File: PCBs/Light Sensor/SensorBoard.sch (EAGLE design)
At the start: 7 parts, among them J1 AVR_SPI_PRG_6NS, U1 TINY85-20-DIP

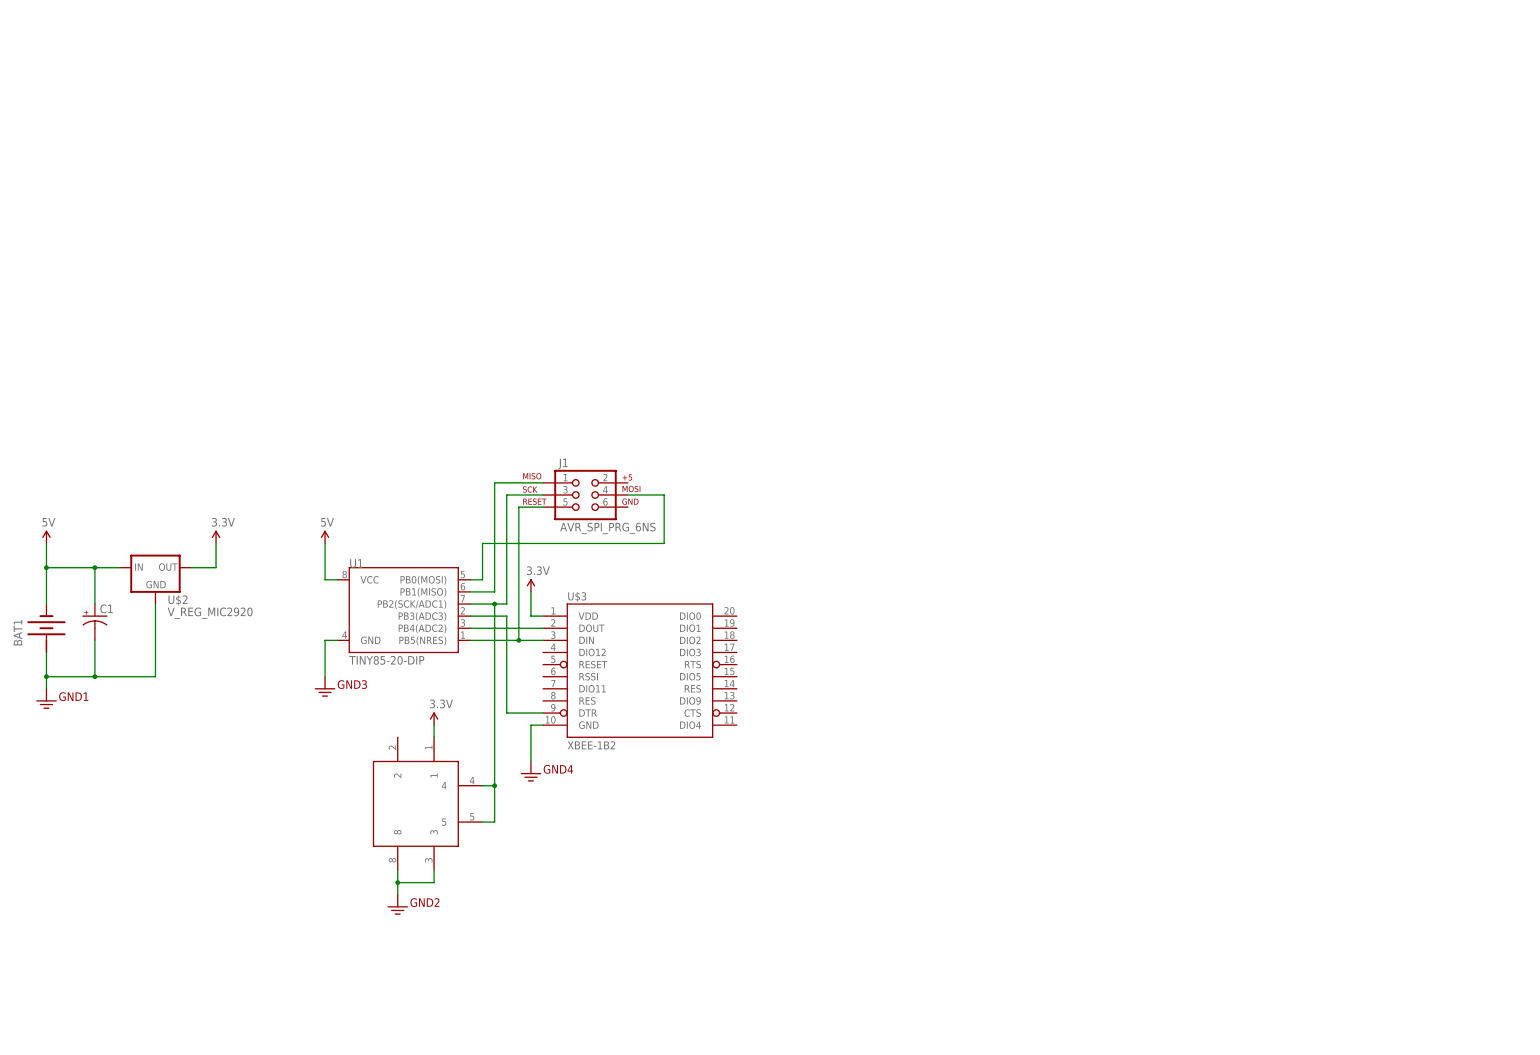
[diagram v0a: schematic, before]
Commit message: Changed to using breadboard friendly symbols
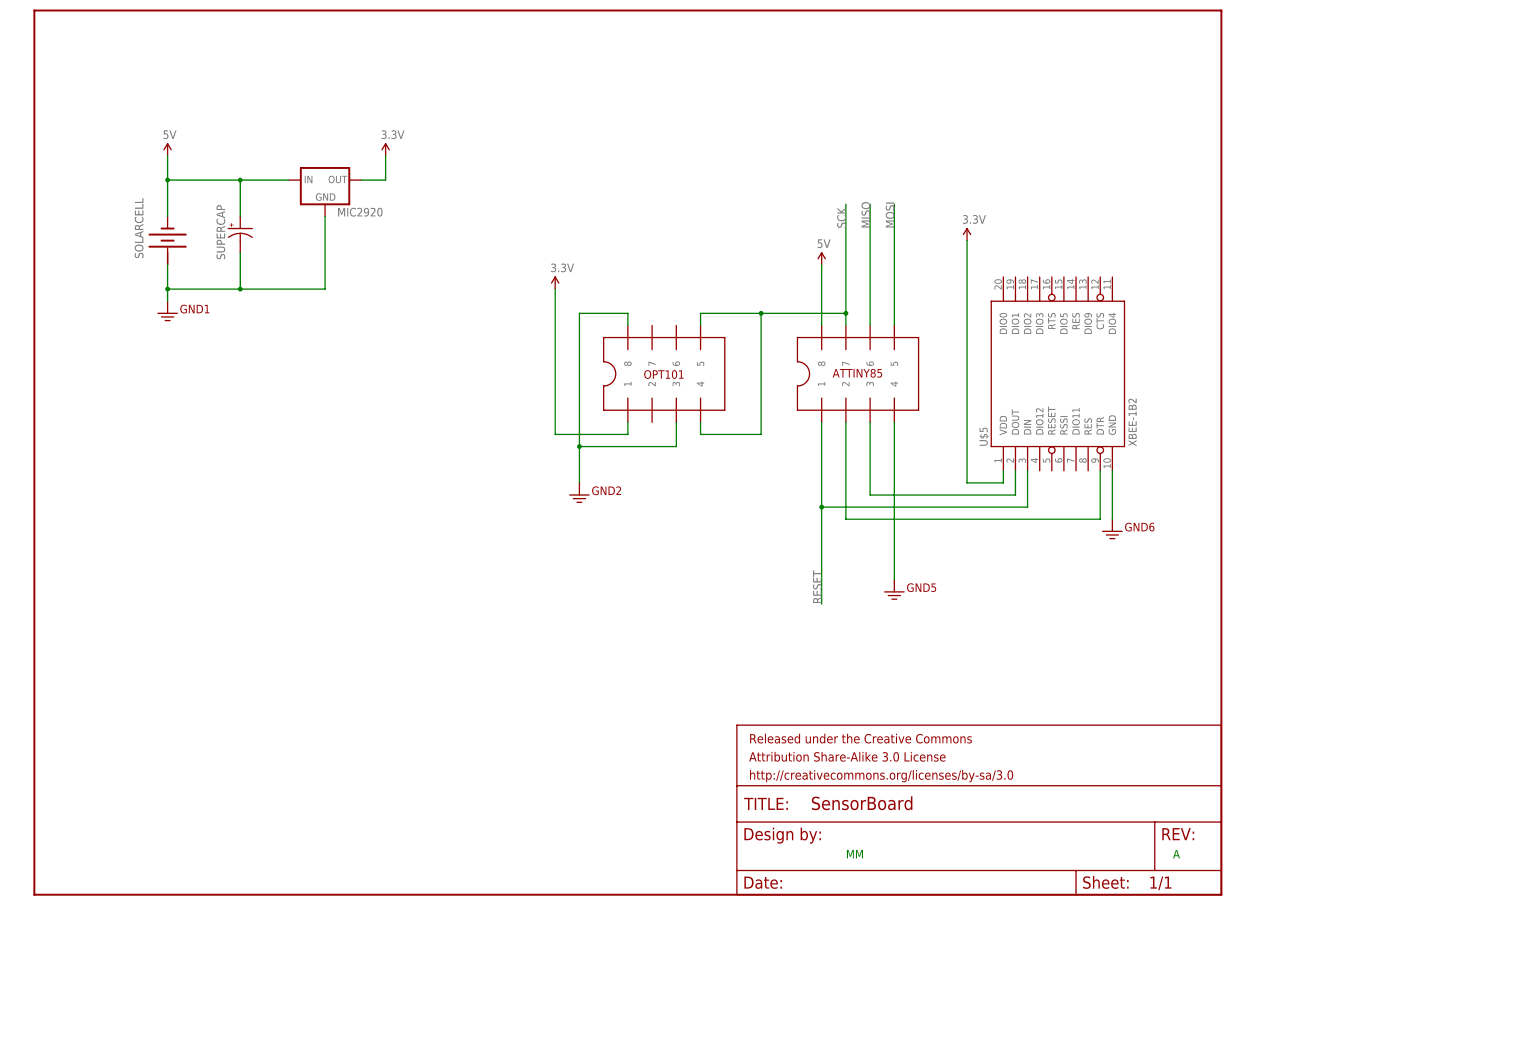
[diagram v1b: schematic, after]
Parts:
- removed BAT1: (no value), special:BATTERY
- removed C1: (no value), rcl:CPOL-USE55-30AXIAL
- removed J1: AVR_SPI_PRG_6NS, SparkFun-Connectors:AVR_SPI_PRG_6NS
- removed U$2: V_REG_MIC2920, SparkFun-PowerIC:V_REG_MIC2920
- removed U$3: XBEE-1B2, SparkFun-RF:XBEE-1B2
- removed U1: TINY85-20-DIP, SparkFun-DigitalIC:ATTINY45TINY85-20-DIP
- added FRAME1: FRAME-LETTER, SparkFun-Aesthetics:FRAME-LETTER
- added MIC2920: V_REG_MIC2920, SparkFun-PowerIC:V_REG_MIC2920
- added SOLARCELL: (no value), special:BATTERY
- added SUPERCAP: (no value), rcl:CPOL-USE55-30AXIAL
- added U$4: ATTINY85, MyLibrary:ATTINY85
- added U$5: XBEE-1B2, SparkFun-RF:XBEE-1B2
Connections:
- removed net N$1: U$3.DOUT, U1.PB4(ADC2)
- removed net N$2: J1.3, U$1.4, U$1.5, U1.PB2(SCK/ADC1)
- removed net N$3: J1.5, U$3.DIN, U1.PB5(NRES)
- removed net N$4: U$3.DTR, U1.PB3(ADC3)
- removed net N$5: J1.1, U1.PB1(MISO)
- removed net N$7: J1.4, U1.PB0(MOSI)
- new net MISO: U$4.6
- new net MOSI: U$4.5
- new net N$10: U$4.3, U$5.DOUT
- new net N$8: U$4.2, U$5.DTR
- new net RESET: U$4.1, U$5.DIN
- new net SCK: U$1.4, U$1.5, U$4.7
- net 3.3V: now also MIC2920.GND, MIC2920.OUT, SOLARCELL.+, SUPERCAP.-, U$4.4, U$5.GND, U$5.VDD; no longer BAT1.+, C1.-, U$2.GND, U$2.OUT, U$3.GND, U$3.VDD, U1.GND
- net 5V: now also MIC2920.IN, SOLARCELL.-, SUPERCAP.+, U$4.8; no longer BAT1.-, C1.+, U$2.IN, U1.VCC
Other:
- note added: "A"
- note added: "MM"

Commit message: Added level translator, jumpers
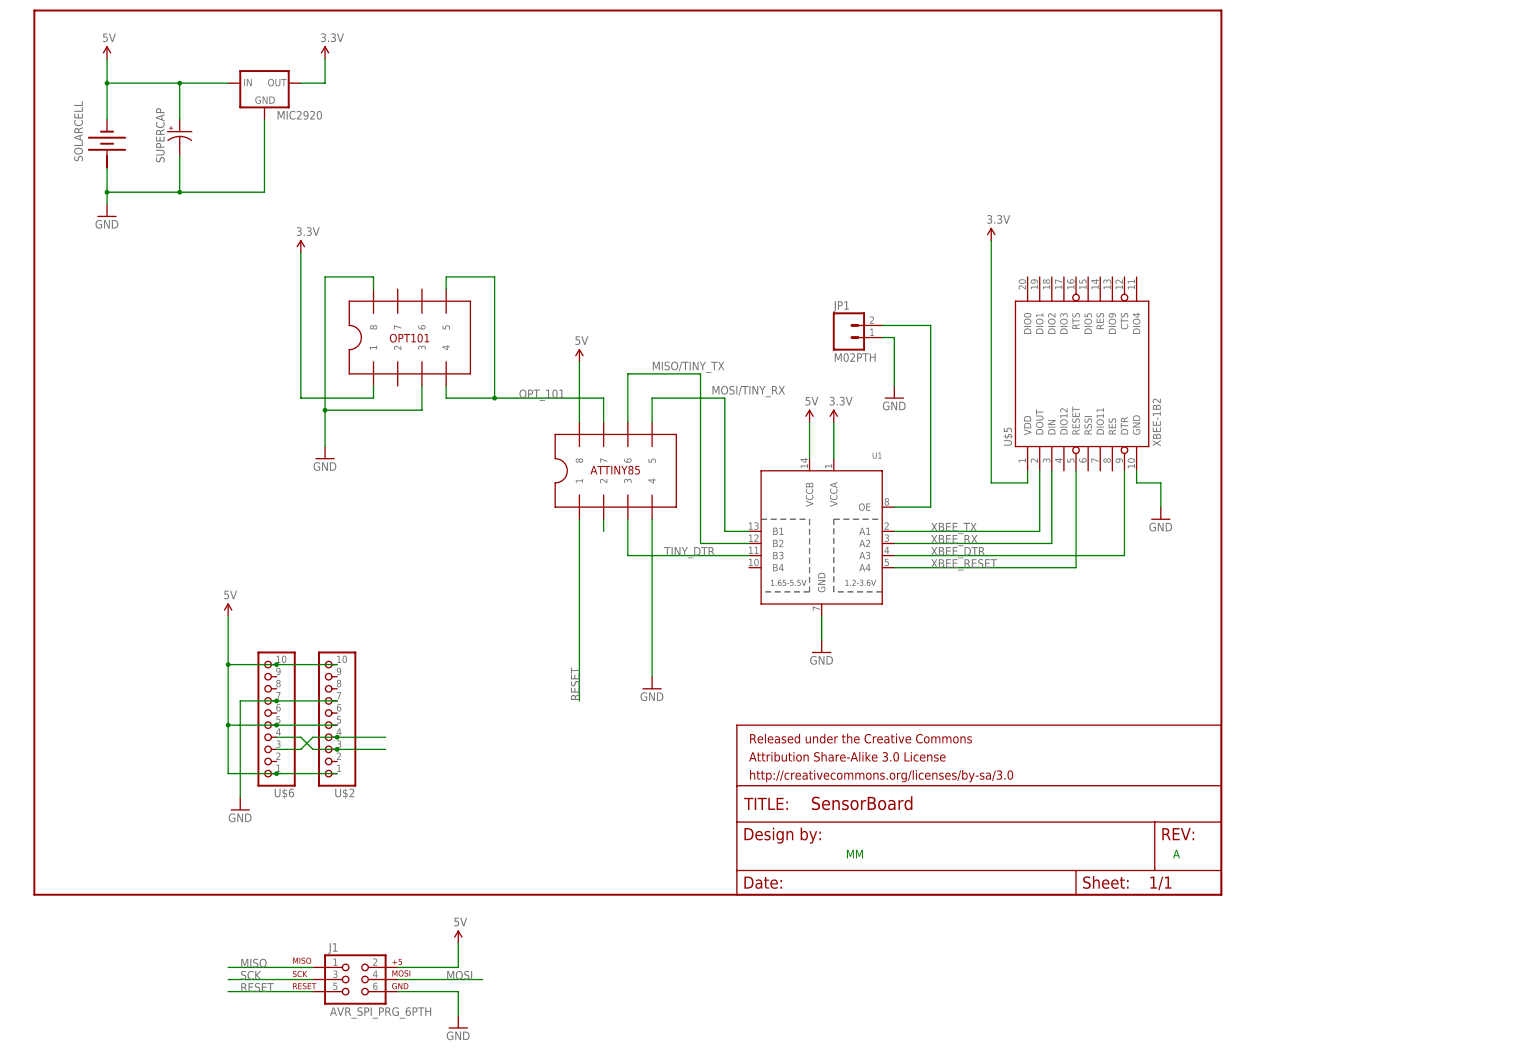
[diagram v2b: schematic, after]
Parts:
- added J1: AVR_SPI_PRG_6PTH, SparkFun-Connectors:AVR_SPI_PRG_6PTH
- added JP1: M02PTH, SparkFun-Connectors:M02PTH
- added U$2, U$6: PINHD-1X10, adafruit:PINHD-1X10
- added U1: (no value), SparkFun-DigitalIC:TXB0104PWRSOIC14
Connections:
- removed net N$10: U$4.3, U$5.DOUT
- removed net N$8: U$4.2, U$5.DTR
- new net GND: J1.6, JP1.1, MIC2920.GND, SOLARCELL.+, SUPERCAP.-, U$1.3, U$1.8, U$2.7, U$4.4, U$5.GND, U$6.7, U1.GND
- new net MISO/TINY_TX: U$4.6, U1.B2
- new net MOSI/TINY_RX: U$4.5, U1.B1
- new net N$2: U$2.3, U$6.4
- new net N$3: U$2.4, U$6.3
- new net N$5: JP1.2, U1.OE
- new net OPT_101: U$1.4, U$1.5, U$4.7
- new net TINY_DTR: U$4.3, U1.B3
- new net XBEE_DTR: U$4.2, U$5.DTR, U1.A3
- new net XBEE_RESET: U$5.RESET, U1.A4
- new net XBEE_RX: U$5.DIN, U1.A2
- new net XBEE_TX: U$5.DOUT, U1.A1
- net 3.3V: now also U1.VCCA; no longer MIC2920.GND, SOLARCELL.+, SUPERCAP.-, U$1.3, U$1.8, U$4.4, U$5.GND
- net 5V: now also J1.2, U$2.1, U$2.10, U$2.5, U$6.1, U$6.10, U$6.5, U1.VCCB
- net MISO: now also J1.1; no longer U$4.6
- net MOSI: now also J1.4; no longer U$4.5
- net RESET: now also J1.5; no longer U$5.DIN
- net SCK: now also J1.3; no longer U$1.4, U$1.5, U$4.7
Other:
- moved on the sheet: MIC2920, SOLARCELL, SUPERCAP, U$5

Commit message: Cleanups
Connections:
- removed net MISO: J1.1
- removed net MOSI: J1.4
- net MISO/TINY_TX: now also J1.1
- net MOSI/TINY_RX: now also J1.4
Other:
- moved on the sheet: J1
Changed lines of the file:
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@@
 <instance part="FRAME1" gate="G$1" x="0" y="0"/>
 <instance part="FRAME1" gate="G$2" x="147.32" y="0"/>
-<instance part="J1" gate="G$1" x="66.04" y="-17.78"/>
-<instance part="SUPPLY4" gate="G$1" x="88.9" y="-10.16"/>
+<instance part="J1" gate="G$1" x="129.54" y="160.02"/>
+<instance part="SUPPLY4" gate="G$1" x="152.4" y="167.64"/>
 <instance part="GND1" gate="1" x="15.24" y="142.24"/>
 <instance part="GND2" gate="1" x="60.96" y="91.44"/>
-<instance part="GND3" gate="1" x="88.9" y="-27.94"/>
+<instance part="GND3" gate="1" x="152.4" y="149.86"/>
 <instance part="GND4" gate="1" x="129.54" y="43.18"/>
 <instance part="GND5" gate="1" x="236.22" y="78.74"/>
@@
 <segment>
 <pinref part="J1" gate="G$1" pin="2"/>
-<wire x1="76.2" y1="-15.24" x2="88.9" y2="-15.24" width="0.1524" layer="91"/>
+<wire x1="139.7" y1="162.56" x2="152.4" y2="162.56" width="0.1524" layer="91"/>
 <pinref part="SUPPLY4" gate="G$1" pin="5V"/>
-<wire x1="88.9" y1="-10.16" x2="88.9" y2="-15.24" width="0.1524" layer="91"/>
+<wire x1="152.4" y1="167.64" x2="152.4" y2="162.56" width="0.1524" layer="91"/>
 </segment>
 <segment>
@@
 <segment>
 <pinref part="J1" gate="G$1" pin="3"/>
-<wire x1="58.42" y1="-17.78" x2="40.64" y2="-17.78" width="0.1524" layer="91"/>
-<label x="43.18" y="-17.78" size="1.778" layer="95"/>
+<wire x1="121.92" y1="160.02" x2="93.98" y2="160.02" width="0.1524" layer="91"/>
+<label x="96.52" y="160.02" size="1.778" layer="95"/>
 </segment>
 </net>
@@
 <segment>
 <pinref part="J1" gate="G$1" pin="5"/>
-<wire x1="58.42" y1="-20.32" x2="40.64" y2="-20.32" width="0.1524" layer="91"/>
-<label x="43.18" y="-20.32" size="1.778" layer="95"/>
-</segment>
-</net>
-<net name="MISO" class="0">
-<segment>
-<pinref part="J1" gate="G$1" pin="1"/>
-<wire x1="58.42" y1="-15.24" x2="40.64" y2="-15.24" width="0.1524" layer="91"/>
-<label x="43.18" y="-15.24" size="1.778" layer="95"/>
-</segment>
-</net>
-<net name="MOSI" class="0">
-<segment>
-<pinref part="J1" gate="G$1" pin="4"/>
-<wire x1="76.2" y1="-17.78" x2="93.98" y2="-17.78" width="0.1524" layer="91"/>
-<label x="86.36" y="-17.78" size="1.778" layer="95"/>
+<wire x1="121.92" y1="157.48" x2="93.98" y2="157.48" width="0.1524" layer="91"/>
+<label x="96.52" y="157.48" size="1.778" layer="95"/>
 </segment>
 </net>
@@
 <segment>
 <pinref part="J1" gate="G$1" pin="6"/>
-<wire x1="76.2" y1="-20.32" x2="88.9" y2="-20.32" width="0.1524" layer="91"/>
-<wire x1="88.9" y1="-20.32" x2="88.9" y2="-25.4" width="0.1524" layer="91"/>
+<wire x1="139.7" y1="157.48" x2="152.4" y2="157.48" width="0.1524" layer="91"/>
+<wire x1="152.4" y1="157.48" x2="152.4" y2="152.4" width="0.1524" layer="91"/>
 <pinref part="GND3" gate="1" pin="GND"/>
 </segment>
@@
 <wire x1="144.78" y1="76.2" x2="149.86" y2="76.2" width="0.1524" layer="91"/>
 </segment>
+<segment>
+<pinref part="J1" gate="G$1" pin="4"/>
+<wire x1="139.7" y1="160.02" x2="167.64" y2="160.02" width="0.1524" layer="91"/>
+<label x="149.86" y="160.02" size="1.778" layer="95"/>
+</segment>
 </net>
 <net name="MISO/TINY_TX" class="0">
@@
 <wire x1="139.7" y1="73.66" x2="149.86" y2="73.66" width="0.1524" layer="91"/>
 </segment>
-</net>
+<segment>
+<pinref part="J1" gate="G$1" pin="1"/>
+<wire x1="121.92" y1="162.56" x2="93.98" y2="162.56" width="0.1524" layer="91"/>
+<label x="96.52" y="162.56" size="1.778" layer="95"/>
+</segment>
+</net>

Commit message: Added protection, pinswap level shift, proto area
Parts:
- removed SOLARCELL: (no value), special:BATTERY
- removed SUPERCAP: (no value), rcl:CPOL-USE55-30AXIAL
- added JP2, JP3: M021X02_NO_SILK, SparkFun-Connectors:M021X02_NO_SILK
- added JP4: USBSMD, SparkFun-Connectors:USBSMD
- added JP5, JP6: (no value), SparkFun-Connectors:M031X03_NO_SILK
- added JP7: (no value), SparkFun-Connectors:M041X04_NO_SILK
- added R1, R2: (no value), SparkFun-Passives:RESISTORAXIAL-0.3
- added U$3: APDS-9008, MyLibrary:APDS-9008
- added U$7: FYD0H225ZF, MyLibrary:FYD0H225ZF
- added U$8: PROTOAREA-10X10, MyLibrary:PROTOAREA-10X10
- U$1: value OPT101 -> OPT101SMD; device MyLibrary:OPT101 -> MyLibrary:OPT101SMD
- U$4: value ATTINY85 -> ATTINY85SMD; device MyLibrary:ATTINY85 -> MyLibrary:ATTINY85SMD
- U$5: value XBEE-1B2 -> XBEE-1B1; device SparkFun-RF:XBEE-1B2 -> MyLibrary:XBEE-1B1
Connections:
- new net APDS_9008: U$3.OUT, U$4.2
- new net N$1: JP4.VBUS, R1.1
- new net N$4: R2.1, U$2.1, U$2.10, U$2.5, U$6.1, U$6.10, U$6.5
- net 3.3V: now also JP6.1, JP6.2, JP6.3, U$3.VCC
- net 5V: now also JP2.1, JP3.1, JP5.1, JP5.2, JP5.3, R1.2, R2.2, U$7.+; no longer SOLARCELL.-, SUPERCAP.+, U$2.1, U$2.10, U$2.5, U$6.1, U$6.10, U$6.5
- net GND: now also JP2.2, JP3.2, JP4.GND, JP7.1, JP7.2, JP7.3, JP7.4, U$3.GND, U$7.-; no longer SOLARCELL.+, SUPERCAP.-
- net MISO/TINY_TX: now also U1.B3; no longer U1.B2
- net MOSI/TINY_RX: now also U1.B4; no longer U1.B1
- net RESET: now also U1.B2
- net TINY_DTR: now also U1.B1; no longer U1.B3
- net XBEE_DTR: now also U1.A1; no longer U$4.2, U1.A3
- net XBEE_RESET: now also U1.A2; no longer U1.A4
- net XBEE_RX: now also U1.A3; no longer U1.A2
- net XBEE_TX: now also U1.A4; no longer U1.A1
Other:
- moved on the sheet: MIC2920, U$2, U$6
